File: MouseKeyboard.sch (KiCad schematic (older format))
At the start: 12 parts

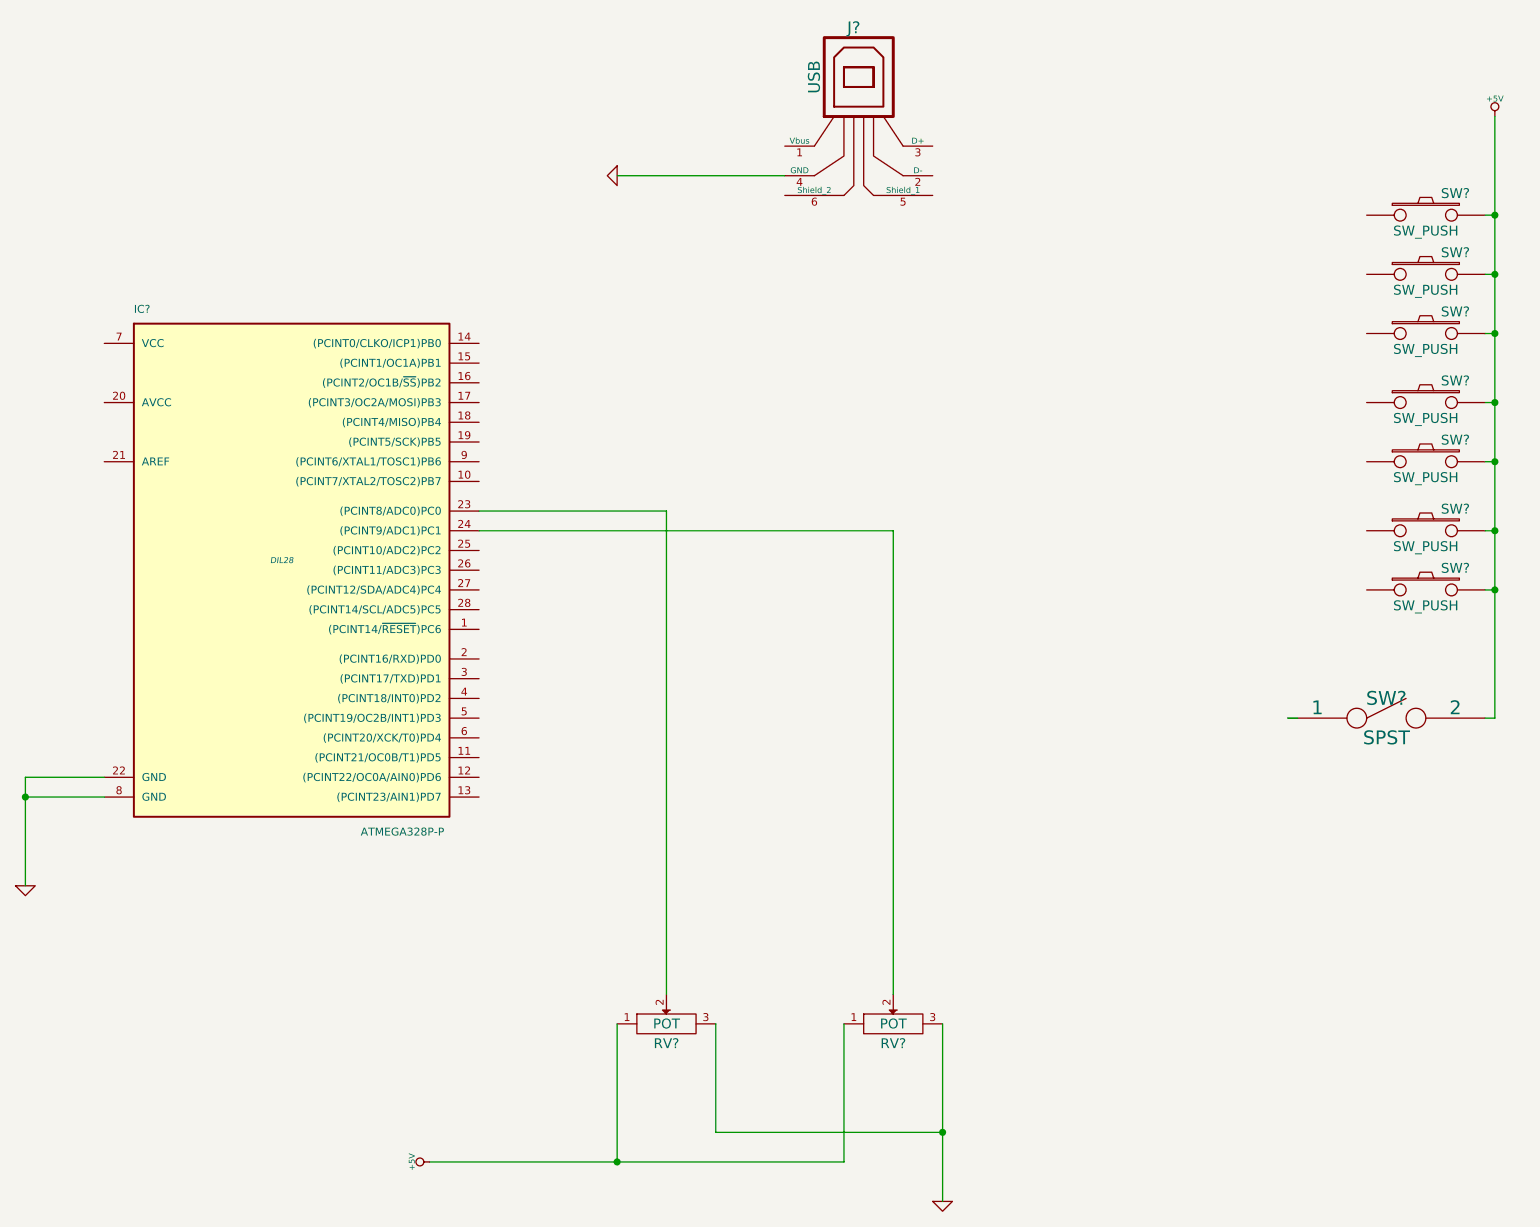
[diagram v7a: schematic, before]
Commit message: Started Filling out the usb port
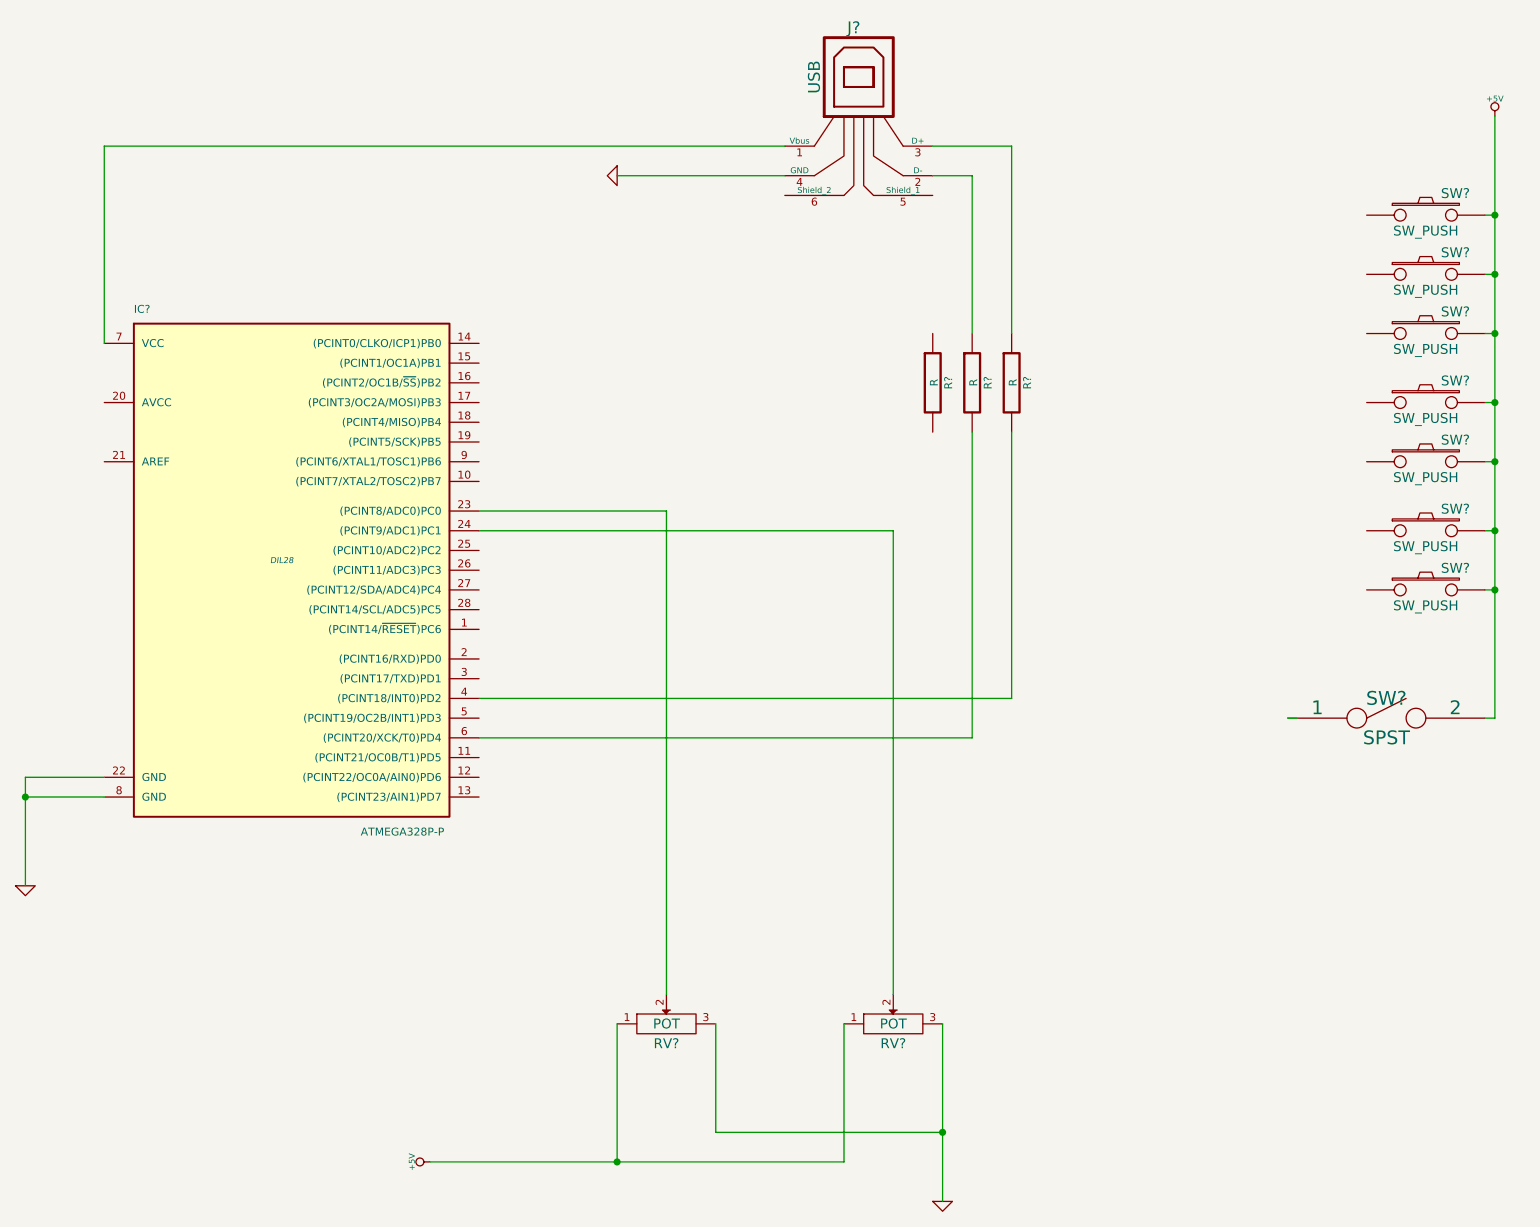
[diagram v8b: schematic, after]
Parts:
- added R? (x3): R, symbol R
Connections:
- wire segments 24 -> 34
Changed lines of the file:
@@
 Wire Wire Line
 	5050 1550 4200 1550
+$Comp
+L R R?
+U 1 1 54DD4896
+P 5800 2600
+F 0 "R?" V 5880 2600 40  0000 C CNN
+F 1 "R" V 5807 2601 40  0000 C CNN
+F 2 "" V 5730 2600 30  0000 C CNN
+F 3 "" H 5800 2600 30  0000 C CNN
+	1    5800 2600
+	1    0    0    -1
+$EndComp
+$Comp
+L R R?
+U 1 1 54DD48AA
+P 6000 2600
+F 0 "R?" V 6080 2600 40  0000 C CNN
+F 1 "R" V 6007 2601 40  0000 C CNN
+F 2 "" V 5930 2600 30  0000 C CNN
+F 3 "" H 6000 2600 30  0000 C CNN
+	1    6000 2600
+	1    0    0    -1
+$EndComp
+$Comp
+L R R?
+U 1 1 54DD48BE
+P 6200 2600
+F 0 "R?" V 6280 2600 40  0000 C CNN
+F 1 "R" V 6207 2601 40  0000 C CNN
+F 2 "" V 6130 2600 30  0000 C CNN
+F 3 "" H 6200 2600 30  0000 C CNN
+	1    6200 2600
+	1    0    0    -1
+$EndComp
+Wire Wire Line
+	5050 1400 1600 1400
+Wire Wire Line
+	1600 1400 1600 2400
+Wire Wire Line
+	3500 4200 6200 4200
+Wire Wire Line
+	6200 1400 5800 1400
+Wire Wire Line
+	6200 2350 6200 1400
+Wire Wire Line
+	6200 4200 6200 2850
+Wire Wire Line
+	5800 1550 6000 1550
+Wire Wire Line
+	6000 1550 6000 2350
+Wire Wire Line
+	3500 4400 6000 4400
+Wire Wire Line
+	6000 4400 6000 2850
 $EndSCHEMATC
